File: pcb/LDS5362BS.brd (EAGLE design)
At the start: 40.3 x 35.6 mm, 11 parts

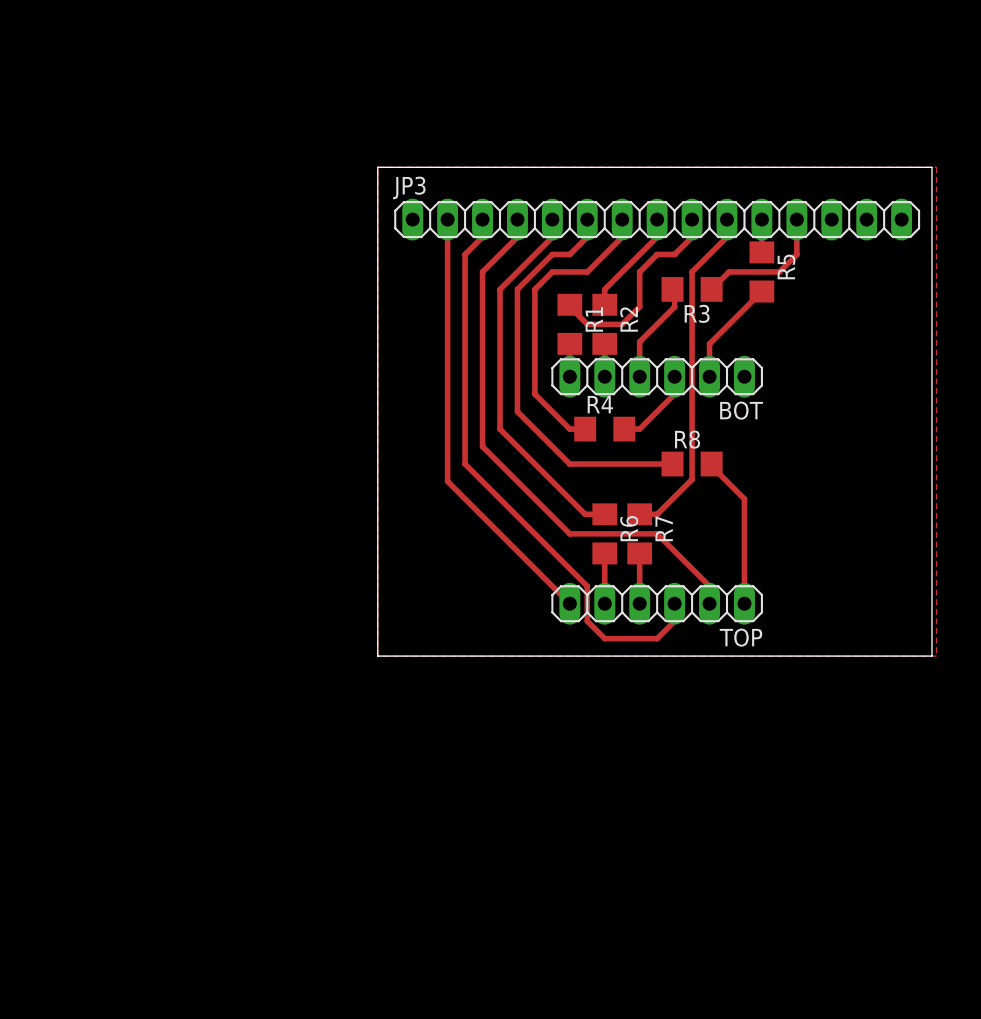
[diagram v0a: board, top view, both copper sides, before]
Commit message: Updated the schematic with ATmega8 & passives.
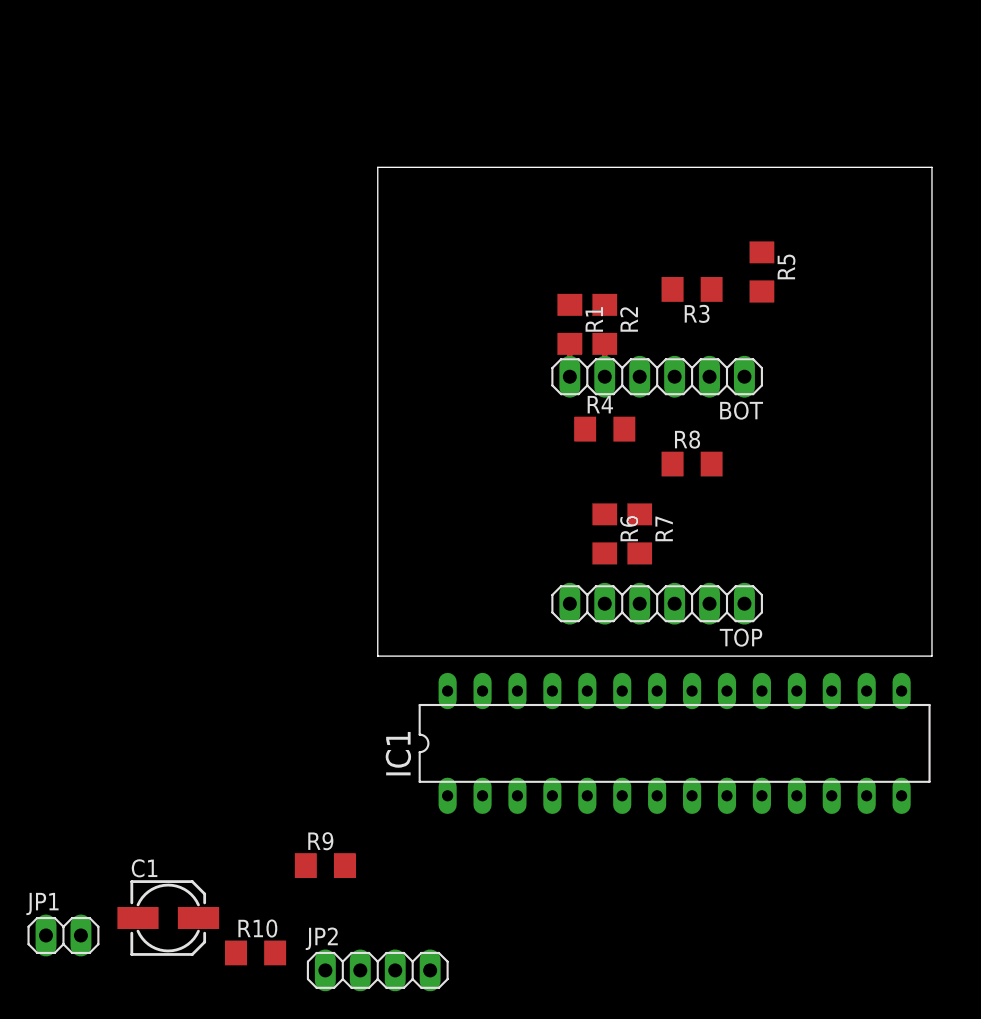
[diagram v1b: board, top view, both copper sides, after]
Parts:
- removed JP3: (no value), pinhead:1X15
- added C1: (no value), rcl:153CLV-0505
- added IC1: MEGA8-P, atmel:DIL28-3
- added JP1: (no value), pinhead:1X02
- added JP2: (no value), pinhead:1X04
- added R10, R9: 4k7, resistor:R1206
- R1, R2, R3, R4, R5, R6, R7, R8: value (none) -> 1k5
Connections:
- removed net BTN_DOWN: JP3.13
- removed net BTN_UP: JP3.14
- new net AVCC: IC1.20
- new net N$9: IC1.1, R9.2
- new net TEMP: IC1.23, JP2.4, R10.2
- net A: now also IC1.13; no longer JP3.5
- net B: now also IC1.12; no longer JP3.6
- net C: now also IC1.11; no longer JP3.7
- net D: now also IC1.5; no longer JP3.8
- net DP: now also IC1.6; no longer JP3.12
- net E: now also IC1.4; no longer JP3.9
- net F: now also IC1.3; no longer JP3.10
- net G: now also IC1.2; no longer JP3.11
- net GND: now also C1.-, IC1.22, IC1.8, JP1.2, JP2.2; no longer JP3.15
- net LEFT: now also IC1.14; no longer JP3.2
- net MIDDLE: now also IC1.15; no longer JP3.3
- net RIGHT: now also IC1.16; no longer JP3.4
- net VCC: now also C1.+, IC1.7, JP1.1, JP2.1, R10.1, R9.1; no longer JP3.1
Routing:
- net MIDDLE: track 42.1 -> 0.00 mm
- net RIGHT: track 39.6 -> 0.00 mm
- net LEFT: track 31.6 -> 0.00 mm
- net B: track 29.7 -> 0.00 mm
- net A: track 27.0 -> 0.00 mm
- net F: track 24.8 -> 0.00 mm
- net C: track 21.5 -> 0.00 mm
- net E: track 15.0 -> 0.00 mm
- net N$1: track 12.4 -> 1.27 mm
- net DP: track 9.79 -> 0.00 mm
- net N$4: track 7.78 -> 0.00 mm
- net D: track 7.78 -> 0.00 mm
- net N$6: track 7.47 -> 0.00 mm
- net N$5: track 5.98 -> 0.00 mm
- net N$3: track 3.66 -> 0.00 mm
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- removed copper zone on layer 1, net GND

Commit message: Routed the PCB.
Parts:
- moved JP1 86.2 mm to (40.6, 55.9), turned to 180 degrees
- moved C1 75.5 mm to (40.6, 49.5)
- moved R10 71.0 mm to (26.7, 55.9), turned to 180 degrees
- moved JP2 66.5 mm to (19.1, 55.9)
- moved R9 59.5 mm to (38.1, 44.5), turned to 180 degrees
- moved IC1 41.3 mm to (17.8, 48.3), flipped to the bottom
- moved R6 24.3 mm to (3.81, 40.6)
- moved R8 24.0 mm to (6.35, 40.6), turned to 270 degrees
- moved R4 15.3 mm to (8.89, 40.6), turned to 270 degrees
- moved R3 11.7 mm to (15.2, 38.1), turned to 270 degrees
- moved R7 7.73 mm to (30.5, 21.6), turned to 180 degrees
- moved R2 4.02 mm to (24.1, 39.4)
- moved R5 2.54 mm to (31.8, 39.4)
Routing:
- net RIGHT: track 0.00 -> 69.7 mm
- net VCC: track 0.00 -> 68.8 mm
- net MIDDLE: track 0.00 -> 55.9 mm
- net N$1: track 1.27 -> 37.4 mm
- net LEFT: track 0.00 -> 34.3 mm
- net N$3: track 0.00 -> 28.3 mm
- net F: track 0.00 -> 28.1 mm
- net N$5: track 0.00 -> 24.6 mm
- net N$6: track 0.00 -> 13.6 mm
- net E: track 0.00 -> 13.2 mm
- net DP: track 0.00 -> 9.79 mm
- net N$2: track 0.00 -> 8.52 mm
- net TEMP: track 0.00 -> 6.72 mm
- net N$4: track 0.00 -> 6.07 mm
- net G: track 0.00 -> 3.66 mm
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- added copper zone on layer 1, net GND
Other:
- board size 40.3 x 35.6 mm -> 49.2 x 47 mm
